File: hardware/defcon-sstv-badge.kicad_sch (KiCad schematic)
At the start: 0 parts

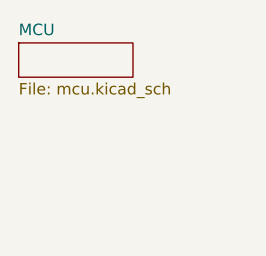
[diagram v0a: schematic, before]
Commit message: add buck/boost
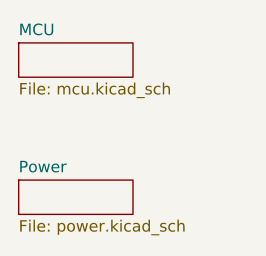
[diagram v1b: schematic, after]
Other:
- added sheet Power (power.kicad_sch)
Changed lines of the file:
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@@
 	(paper "A4")
+	(sheet
+		(at -7.62 55.88)
+		(size 12.7 3.81)
+		(exclude_from_sim no)
+		(in_bom yes)
+		(on_board yes)
+		(dnp no)
+		(fields_autoplaced yes)
+		(stroke
+			(width 0.1524)
+			(type solid)
+		)
+		(fill
+			(color 0 0 0 0.0000)
+		)
+		(property "Sheetname" "Power"
+			(at -7.62 55.1684 0)
+			(effects
+				(font
+					(size 1.27 1.27)
+				)
+				(justify left bottom)
+			)
+		)
+		(property "Sheetfile" "power.kicad_sch"
+			(at -7.62 60.2746 0)
+			(effects
+				(font
+					(size 1.27 1.27)
+				)
+				(justify left top)
+			)
+		)
+		(instances
+			(project "defcon-sstv-badge"
+				(path "/6bfeada4-0da3-4bdd-af4a-70929e466b35"
+					(page "3")
+				)
+			)
+		)
+	)
 	(sheet
 		(at -7.62 40.64)

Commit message: RX Filter
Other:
- added sheet Audio (audio.kicad_sch)
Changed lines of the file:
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@@
 	(paper "A4")
 	(sheet
-		(at -7.62 55.88)
+		(at 80.01 57.658)
 		(size 12.7 3.81)
 		(exclude_from_sim no)
@@
 		)
 		(property "Sheetname" "Power"
-			(at -7.62 55.1684 0)
+			(at 80.01 56.9464 0)
 			(effects
 				(font
@@
 		)
 		(property "Sheetfile" "power.kicad_sch"
-			(at -7.62 60.2746 0)
+			(at 80.01 62.0526 0)
 			(effects
 				(font
@@
 	)
 	(sheet
-		(at -7.62 40.64)
+		(at 79.756 45.466)
 		(size 12.7 3.81)
 		(exclude_from_sim no)
@@
 		)
 		(property "Sheetname" "MCU"
-			(at -7.62 39.9284 0)
+			(at 79.756 44.7544 0)
 			(effects
 				(font
@@
 		)
 		(property "Sheetfile" "mcu.kicad_sch"
-			(at -7.62 45.0346 0)
+			(at 79.756 49.8606 0)
 			(effects
 				(font
@@
 				)
 			)
+		)
+	)
+	(sheet
+		(at 80.518 71.12)
+		(size 12.7 3.81)
+		(exclude_from_sim no)
+		(in_bom yes)
+		(on_board yes)
+		(dnp no)
+		(fields_autoplaced yes)
+		(stroke
+			(width 0.1524)
+			(type solid)
+		)
+		(fill
+			(color 0 0 0 0.0000)
+		)
+		(property "Sheetname" "Audio"
+			(at 80.518 70.4084 0)
+			(effects
+				(font
+					(size 1.27 1.27)
+				)
+				(justify left bottom)
+			)
+		)
+		(property "Sheetfile" "audio.kicad_sch"
+			(at 80.518 75.5146 0)
+			(effects
+				(font
+					(size 1.27 1.27)
+				)
+				(justify left top)
+			)
+		)
+		(instances
+			(project "defcon-sstv-badge"
+				(path "/6bfeada4-0da3-4bdd-af4a-70929e466b35"
+					(page "4")
+				)
+			)

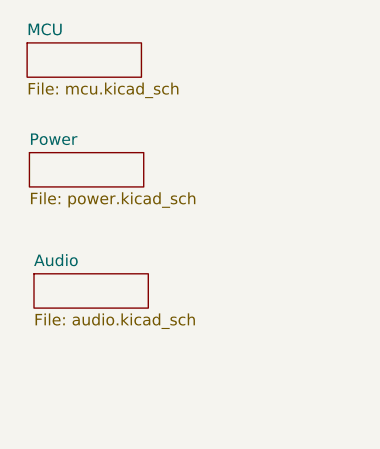
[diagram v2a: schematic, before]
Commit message: camera/display sheet
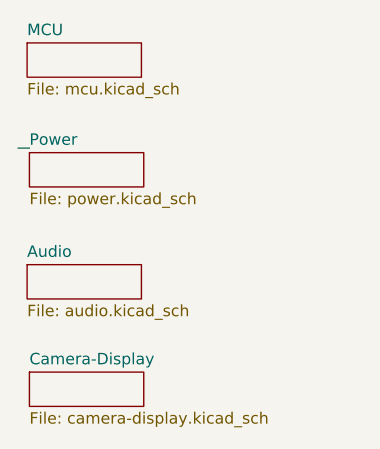
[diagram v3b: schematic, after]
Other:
- added sheet Camera-Display (camera-display.kicad_sch)
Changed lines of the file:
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@@
 	(generator_version "9.0")
 	(paper "A4")
+	(wire
+		(pts
+			(xy 78.74 57.15) (xy 80.01 57.15)
+		)
+		(stroke
+			(width 0)
+			(type default)
+		)
+	)
 	(sheet
 		(at 80.01 57.658)
@@
 	)
 	(sheet
-		(at 80.518 71.12)
+		(at 79.756 70.104)
 		(size 12.7 3.81)
 		(exclude_from_sim no)
@@
 		)
 		(property "Sheetname" "Audio"
-			(at 80.518 70.4084 0)
+			(at 79.756 69.3924 0)
 			(effects
 				(font
@@
 		)
 		(property "Sheetfile" "audio.kicad_sch"
-			(at 80.518 75.5146 0)
+			(at 79.756 74.4986 0)
 			(effects
 				(font
@@
 				)
 			)
+		)
+	)
+	(sheet
+		(at 80.01 82.042)
+		(size 12.7 3.81)
+		(exclude_from_sim no)
+		(in_bom yes)
+		(on_board yes)
+		(dnp no)
+		(fields_autoplaced yes)
+		(stroke
+			(width 0.1524)
+			(type solid)
+		)
+		(fill
+			(color 0 0 0 0.0000)
+		)
+		(property "Sheetname" "Camera-Display"
+			(at 80.01 81.3304 0)
+			(effects
+				(font
+					(size 1.27 1.27)
+				)
+				(justify left bottom)
+			)
+		)
+		(property "Sheetfile" "camera-display.kicad_sch"
+			(at 80.01 86.4366 0)
+			(effects
+				(font
+					(size 1.27 1.27)
+				)
+				(justify left top)
+			)
+		)
+		(instances
+			(project "defcon-sstv-badge"
+				(path "/6bfeada4-0da3-4bdd-af4a-70929e466b35"
+					(page "5")
+				)
+			)

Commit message: Buttons and LEDs
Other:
- added sheet Switches (switches.kicad_sch)
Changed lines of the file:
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@@
+	)
+	(sheet
+		(at 80.264 92.202)
+		(size 12.7 3.81)
+		(exclude_from_sim no)
+		(in_bom yes)
+		(on_board yes)
+		(dnp no)
+		(fields_autoplaced yes)
+		(stroke
+			(width 0.1524)
+			(type solid)
+		)
+		(fill
+			(color 0 0 0 0.0000)
+		)
+		(property "Sheetname" "Switches"
+			(at 80.264 91.4904 0)
+			(effects
+				(font
+					(size 1.27 1.27)
+				)
+				(justify left bottom)
+			)
+		)
+		(property "Sheetfile" "switches.kicad_sch"
+			(at 80.264 96.5966 0)
+			(effects
+				(font
+					(size 1.27 1.27)
+				)
+				(justify left top)
+			)
+		)
+		(instances
+			(project "defcon-sstv-badge"
+				(path "/6bfeada4-0da3-4bdd-af4a-70929e466b35"
+					(page "6")
+				)
+			)
+		)
 	)
 	(sheet

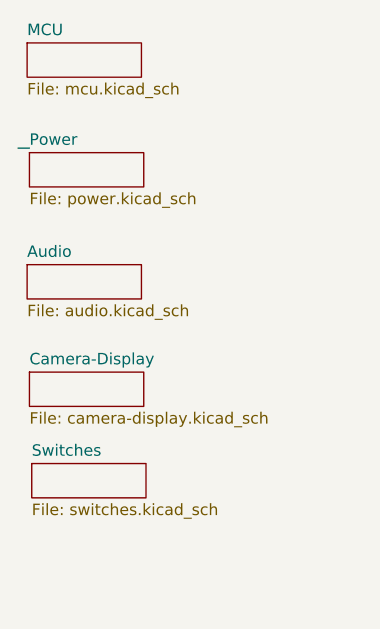
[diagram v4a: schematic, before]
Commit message: all design sheets complete, ERC clean
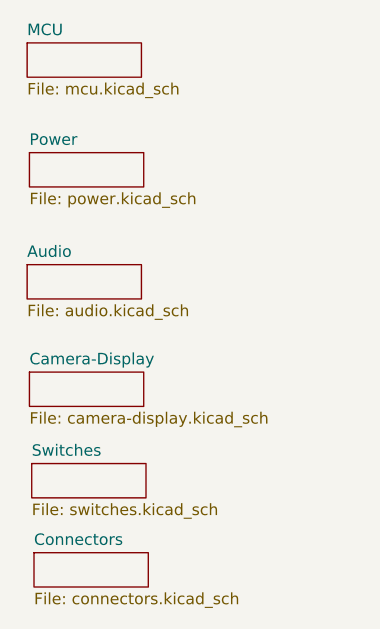
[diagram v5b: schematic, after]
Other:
- added sheet Connectors (connectors.kicad_sch)
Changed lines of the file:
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@@
 	(generator_version "9.0")
 	(paper "A4")
-	(wire
-		(pts
-			(xy 78.74 57.15) (xy 80.01 57.15)
-		)
-		(stroke
-			(width 0)
-			(type default)
-		)
-	)
 	(sheet
 		(at 80.01 57.658)
@@
 				)
 			)
+		)
+	)
+	(sheet
+		(at 80.518 102.108)
+		(size 12.7 3.81)
+		(exclude_from_sim no)
+		(in_bom yes)
+		(on_board yes)
+		(dnp no)
+		(fields_autoplaced yes)
+		(stroke
+			(width 0.1524)
+			(type solid)
+		)
+		(fill
+			(color 0 0 0 0.0000)
+		)
+		(property "Sheetname" "Connectors"
+			(at 80.518 101.3964 0)
+			(effects
+				(font
+					(size 1.27 1.27)
+				)
+				(justify left bottom)
+			)
+		)
+		(property "Sheetfile" "connectors.kicad_sch"
+			(at 80.518 106.5026 0)
+			(effects
+				(font
+					(size 1.27 1.27)
+				)
+				(justify left top)
+			)
+		)
+		(instances
+			(project "defcon-sstv-badge"
+				(path "/6bfeada4-0da3-4bdd-af4a-70929e466b35"
+					(page "7")
+				)
+			)

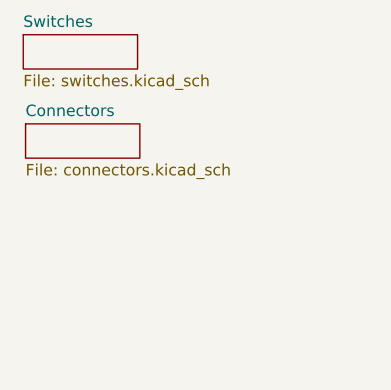
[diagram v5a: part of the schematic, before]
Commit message: add carrier boards for SA818 modules
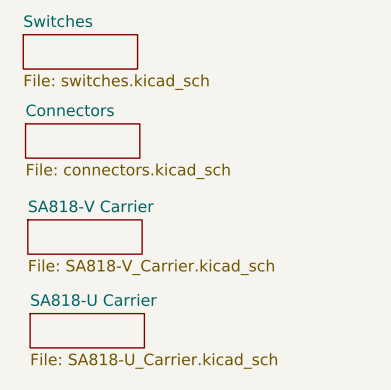
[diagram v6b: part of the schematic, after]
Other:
- added sheet SA818-U Carrier (SA818-U_Carrier.kicad_sch)
- added sheet SA818-V Carrier (SA818-V_Carrier.kicad_sch)
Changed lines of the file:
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@@
 	(paper "A4")
+	(sheet
+		(at 81.026 123.19)
+		(size 12.7 3.81)
+		(exclude_from_sim no)
+		(in_bom yes)
+		(on_board yes)
+		(dnp no)
+		(fields_autoplaced yes)
+		(stroke
+			(width 0.1524)
+			(type solid)
+		)
+		(fill
+			(color 0 0 0 0.0000)
+		)
+		(property "Sheetname" "SA818-U Carrier"
+			(at 81.026 122.4784 0)
+			(effects
+				(font
+					(size 1.27 1.27)
+				)
+				(justify left bottom)
+			)
+		)
+		(property "Sheetfile" "SA818-U_Carrier.kicad_sch"
+			(at 81.026 127.5846 0)
+			(effects
+				(font
+					(size 1.27 1.27)
+				)
+				(justify left top)
+			)
+		)
+		(instances
+			(project "defcon-sstv-badge"
+				(path "/6bfeada4-0da3-4bdd-af4a-70929e466b35"
+					(page "9")
+				)
+			)
+		)
+	)
+	(sheet
+		(at 80.772 112.776)
+		(size 12.7 3.81)
+		(exclude_from_sim no)
+		(in_bom yes)
+		(on_board yes)
+		(dnp no)
+		(fields_autoplaced yes)
+		(stroke
+			(width 0.1524)
+			(type solid)
+		)
+		(fill
+			(color 0 0 0 0.0000)
+		)
+		(property "Sheetname" "SA818-V Carrier"
+			(at 80.772 112.0644 0)
+			(effects
+				(font
+					(size 1.27 1.27)
+				)
+				(justify left bottom)
+			)
+		)
+		(property "Sheetfile" "SA818-V_Carrier.kicad_sch"
+			(at 80.772 117.1706 0)
+			(effects
+				(font
+					(size 1.27 1.27)
+				)
+				(justify left top)
+			)
+		)
+		(instances
+			(project "defcon-sstv-badge"
+				(path "/6bfeada4-0da3-4bdd-af4a-70929e466b35"
+					(page "8")
+				)
+			)
+		)
+	)
 	(sheet
 		(at 80.01 57.658)

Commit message: add footprints and break carrier boards out into standalone projects
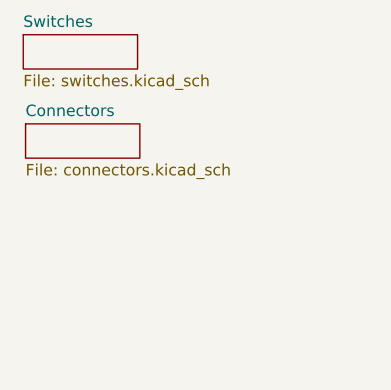
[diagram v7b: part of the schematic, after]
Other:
- removed sheet SA818-U Carrier
- removed sheet SA818-V Carrier
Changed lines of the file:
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@@
 	(paper "A4")
-	(sheet
-		(at 81.026 123.19)
-		(size 12.7 3.81)
-		(exclude_from_sim no)
-		(in_bom yes)
-		(on_board yes)
-		(dnp no)
-		(fields_autoplaced yes)
-		(stroke
-			(width 0.1524)
-			(type solid)
-		)
-		(fill
-			(color 0 0 0 0.0000)
-		)
-		(property "Sheetname" "SA818-U Carrier"
-			(at 81.026 122.4784 0)
-			(effects
-				(font
-					(size 1.27 1.27)
-				)
-				(justify left bottom)
-			)
-		)
-		(property "Sheetfile" "SA818-U_Carrier.kicad_sch"
-			(at 81.026 127.5846 0)
-			(effects
-				(font
-					(size 1.27 1.27)
-				)
-				(justify left top)
-			)
-		)
-		(instances
-			(project "defcon-sstv-badge"
-				(path "/6bfeada4-0da3-4bdd-af4a-70929e466b35"
-					(page "9")
-				)
-			)
-		)
-	)
-	(sheet
-		(at 80.772 112.776)
-		(size 12.7 3.81)
-		(exclude_from_sim no)
-		(in_bom yes)
-		(on_board yes)
-		(dnp no)
-		(fields_autoplaced yes)
-		(stroke
-			(width 0.1524)
-			(type solid)
-		)
-		(fill
-			(color 0 0 0 0.0000)
-		)
-		(property "Sheetname" "SA818-V Carrier"
-			(at 80.772 112.0644 0)
-			(effects
-				(font
-					(size 1.27 1.27)
-				)
-				(justify left bottom)
-			)
-		)
-		(property "Sheetfile" "SA818-V_Carrier.kicad_sch"
-			(at 80.772 117.1706 0)
-			(effects
-				(font
-					(size 1.27 1.27)
-				)
-				(justify left top)
-			)
-		)
-		(instances
-			(project "defcon-sstv-badge"
-				(path "/6bfeada4-0da3-4bdd-af4a-70929e466b35"
-					(page "8")
-				)
-			)
-		)
-	)
 	(sheet
 		(at 80.01 57.658)
